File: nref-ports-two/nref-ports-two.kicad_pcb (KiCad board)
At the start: 2 copper layers, 87.5 x 40.2 mm, 111 parts, among them J1 USB_C_Receptacle, J2 USB_C_Receptacle, J3 USB3_A, J4 HD0919MSMTTR, J5 Conn_01x20, J6 Conn_01x12_Pin, U1 TUSB8041, U10 TPD4E02B04DQA, U11 TPD12S521, U12 LM2830XQMFE/NOPB, U13 LM2830XQMFE/NOPB, U2 HD3SS3220IRNHT, U3 TPD4E02B04DQA, U4 TPD4E02B04DQA, U5 TPD4E02B04DQA, U6 TPD4E02B04DQA, U7 TPD4E02B04DQA, U8 TPD4E02B04DQA, U9 TPD4E02B04DQA, Y1 24MHz

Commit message: ports-two: hdmi routing snapshot
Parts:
- removed R19, R20: 0, Resistor_SMD:R_0402_1005Metric
- added R39: 22k, Resistor_SMD:R_0402_1005Metric, F.Cu at (123.7, 60.5)
- added R40: 22k, Resistor_SMD:R_0402_1005Metric, F.Cu at (123.7, 62.5)
- added R43: 22k, Resistor_SMD:R_0402_1005Metric, F.Cu at (123.7, 64.5)
- added R44: 22k, Resistor_SMD:R_0402_1005Metric, F.Cu at (123.7, 66.5)
- added TP1: TestPoint, TestPoint:TestPoint_Pad_1.0x1.0mm, F.Cu at (126.7, 61.0)
- added TP2: TestPoint, TestPoint:TestPoint_Pad_1.0x1.0mm, F.Cu at (126.7, 64.1)
- H1, H2: value MountingHole_2.2mm_M2_Pad -> MountingHole_Pad
- moved R27 19.6 mm to (109.1, 109.2)
- moved R32 18.5 mm to (109.1, 102.6), turned to 180 degrees
- moved D1 18.4 mm to (107.1, 109.1), turned to -90 degrees
- moved R34 17.1 mm to (109.1, 101.5), turned to 180 degrees
- moved R28 16.7 mm to (109.1, 105.9)
- moved R31 16.4 mm to (109.1, 104.8), turned to 180 degrees
- moved C38 16.3 mm to (121.2, 96.5), turned to 180 degrees
- moved R29 15.4 mm to (109.1, 108.1)
- moved R33 14.7 mm to (109.1, 103.7), turned to 180 degrees
- moved R30 14.6 mm to (109.1, 107.0), turned to 180 degrees
- moved C37 13.0 mm to (121.7, 98.9)
- moved C35 9.71 mm to (122.4, 101.3), turned to -90 degrees
- moved R26 8.41 mm to (121.2, 100.4), turned to -90 degrees
- moved R1 8.33 mm to (110.2, 111.8), turned to 180 degrees
- moved U11 4.77 mm to (116.9, 105.8)
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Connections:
- H1 pad 1: (no net) -> GND
- H2 pad 1: (no net) -> GND
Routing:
- net Net-(J4-CEC): track 0.00 -> 58.8 mm, vias 0 -> 1
- net Net-(J4-SCL): track 0.00 -> 50.3 mm, vias 0 -> 1
- net Net-(J4-HPD): track 0.00 -> 46.1 mm, vias 0 -> 1
- net +5V: track 0.00 -> 39.9 mm, vias 0 -> 2
- net HDMI_TX2N: track 0.00 -> 38.1 mm, vias 0 -> 1
- net Net-(J4-SDA): track 0.00 -> 37.7 mm, vias 0 -> 1
- net HDMI_TX2P: track 0.00 -> 36.2 mm, vias 0 -> 1
- net HDMI_TX0N: track 0.00 -> 36.2 mm
- net HDMI_TX0P: track 0.00 -> 34.4 mm
- net HDMI_TX1P: track 0.00 -> 29.0 mm, vias 0 -> 1
- net HDMI_TX1N: track 0.00 -> 28.2 mm, vias 0 -> 1
- net HDMI_CLKN: track 0.00 -> 25.6 mm, vias 0 -> 1
- net +3V3: track 0.00 -> 25.1 mm, vias 0 -> 2
- net HDMI_CLKP: track 0.00 -> 24.7 mm, vias 0 -> 1
- net GND: track 0.00 -> 23.3 mm, vias 0 -> 21
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- added copper zone on B.Cu, net GND
- added copper zone on F.Cu, net GND
- added copper zone on In1.Cu, net GND
- added copper zone on In2.Cu, net GND
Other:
- copper layers 2 -> 4

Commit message: ports two: usb snapshot
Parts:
- moved R36 55.7 mm to (128.8, 115.7), turned to 180 degrees
- moved C41 55.2 mm to (130.8, 116.7), turned to -90 degrees
- moved U13 52.4 mm to (128.8, 112.7), turned to -90 degrees
- moved R42 49.6 mm to (134.3, 114.2), turned to -90 degrees
- moved D3 49.4 mm to (132.3, 112.7), turned to -90 degrees
- moved R41 46.6 mm to (134.3, 111.7), turned to -90 degrees
- moved L2 45.8 mm to (131.3, 108.7), turned to 0 degrees
- moved TP1 43.6 mm to (131.7, 104.3)
- moved C42 41.7 mm to (135.3, 108.2), turned to 90 degrees
- moved TP2 40.4 mm to (129.6, 104.3)
- moved R39 29.9 mm to (143.2, 83.2), turned to 180 degrees
- moved FB1 29.7 mm to (183.3, 109.8), turned to 0 degrees
- moved C24 29.5 mm to (147.7, 104.6), turned to -90 degrees
- moved C22 28.5 mm to (146.7, 104.6), turned to -90 degrees
- moved R3 27.7 mm to (164.1, 117.2)
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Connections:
- J6 pad 1: USB2A_DN -> USB2_DN
- J6 pad 2: USB2A_DP -> USB2_DP
- U1 pad 19: USBH_1B_TXN -> USBH_2B_TXP
- U1 pad 20: USBH_1B_TXP -> USBH_2B_TXN
- U1 pad 22: USBH_1B_RXN -> USBH_2B_RXN
- U1 pad 23: USBH_1B_RXP -> USBH_2B_RXP
- U1 pad 26: USBH_2B_TXN -> USBH_1B_TXP
- U1 pad 27: USBH_2B_TXP -> USBH_1B_TXN
- U1 pad 29: USBH_2B_RXN -> USBH_1B_RXN
- U1 pad 30: USBH_2B_RXP -> USBH_1B_RXP
- U5 pad 4: /USBH_2B_AC_TXN -> /USBH_2B_AC_TXP
- U5 pad 5: /USBH_2B_AC_TXP -> /USBH_2B_AC_TXN
- U5 pad 6: /USBH_2B_AC_TXP -> /USBH_2B_AC_TXN
- U5 pad 7: /USBH_2B_AC_TXN -> /USBH_2B_AC_TXP
- U9 pad 4: USBH_1A_RXN -> USBH_1A_RXP
- U9 pad 5: USBH_1A_RXP -> USBH_1A_RXN
- U9 pad 6: USBH_1A_RXP -> USBH_1A_RXN
- U9 pad 7: USBH_1A_RXN -> USBH_1A_RXP
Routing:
- net USBH_1_DP: track 0.00 -> 63.6 mm, vias 0 -> 3
- net USBH_1_DN: track 0.00 -> 62.7 mm, vias 0 -> 1
- net USBH_2B_RXP: track 0.00 -> 53.6 mm, vias 0 -> 2
- net USBH_2B_RXN: track 0.00 -> 52.7 mm, vias 0 -> 2
- net USBH_2A_RXN: track 0.00 -> 51.7 mm, vias 0 -> 4
- net USBH_2A_RXP: track 0.00 -> 50.4 mm, vias 0 -> 4
- net /USBH_2B_AC_TXN: track 0.00 -> 47.1 mm, vias 0 -> 2
- net /USBH_2B_AC_TXP: track 0.00 -> 45.6 mm, vias 0 -> 2
- net USBH_2_DN: track 0.00 -> 45.2 mm, vias 0 -> 4
- net USBH_2_DP: track 0.00 -> 42.0 mm, vias 0 -> 2
- net /USBH_2A_AC_TXN: track 0.00 -> 41.8 mm, vias 0 -> 2
- net /USBH_2A_AC_TXP: track 0.00 -> 40.5 mm, vias 0 -> 2
- net USBH_3_DN: track 0.00 -> 32.0 mm, vias 0 -> 2
- net USBH_3_DP: track 0.00 -> 30.3 mm, vias 0 -> 2
- net USBH_1B_RXP: track 0.00 -> 27.1 mm
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
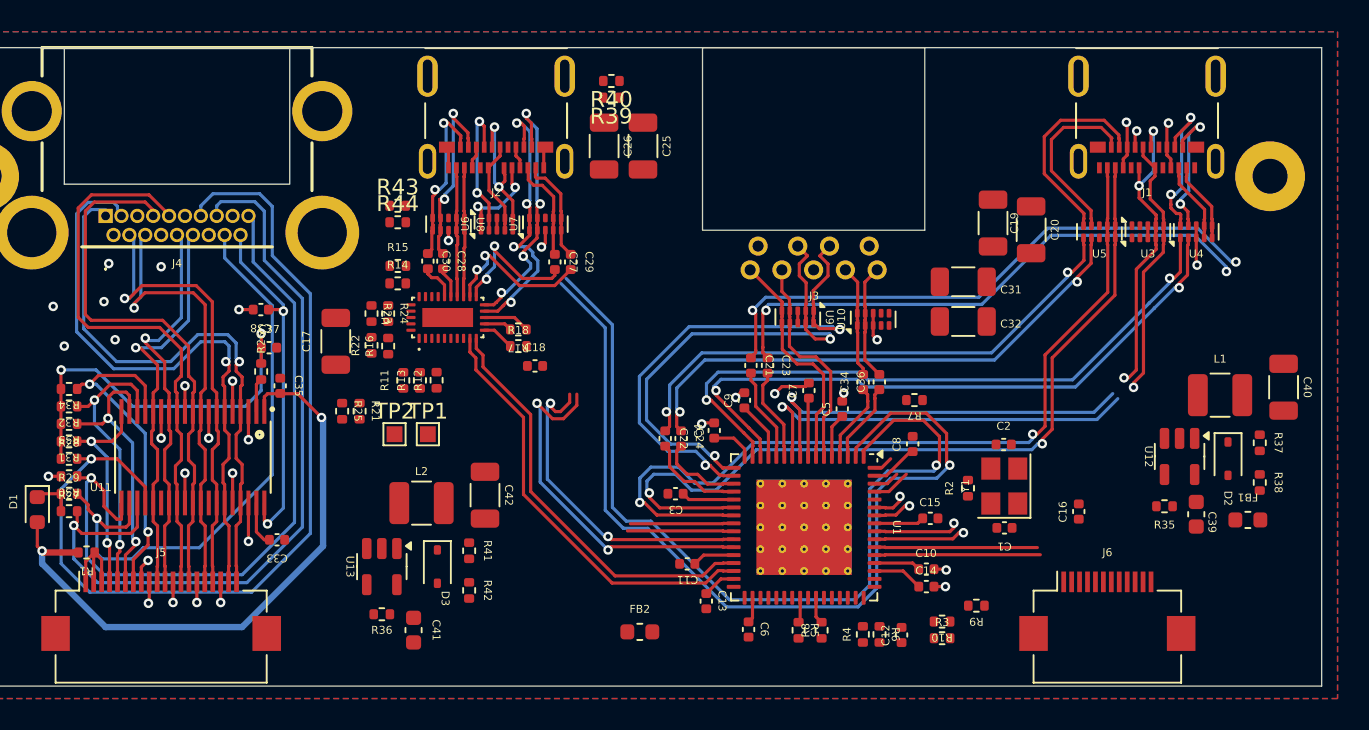
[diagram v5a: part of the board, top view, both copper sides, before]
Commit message: port board two fully routed
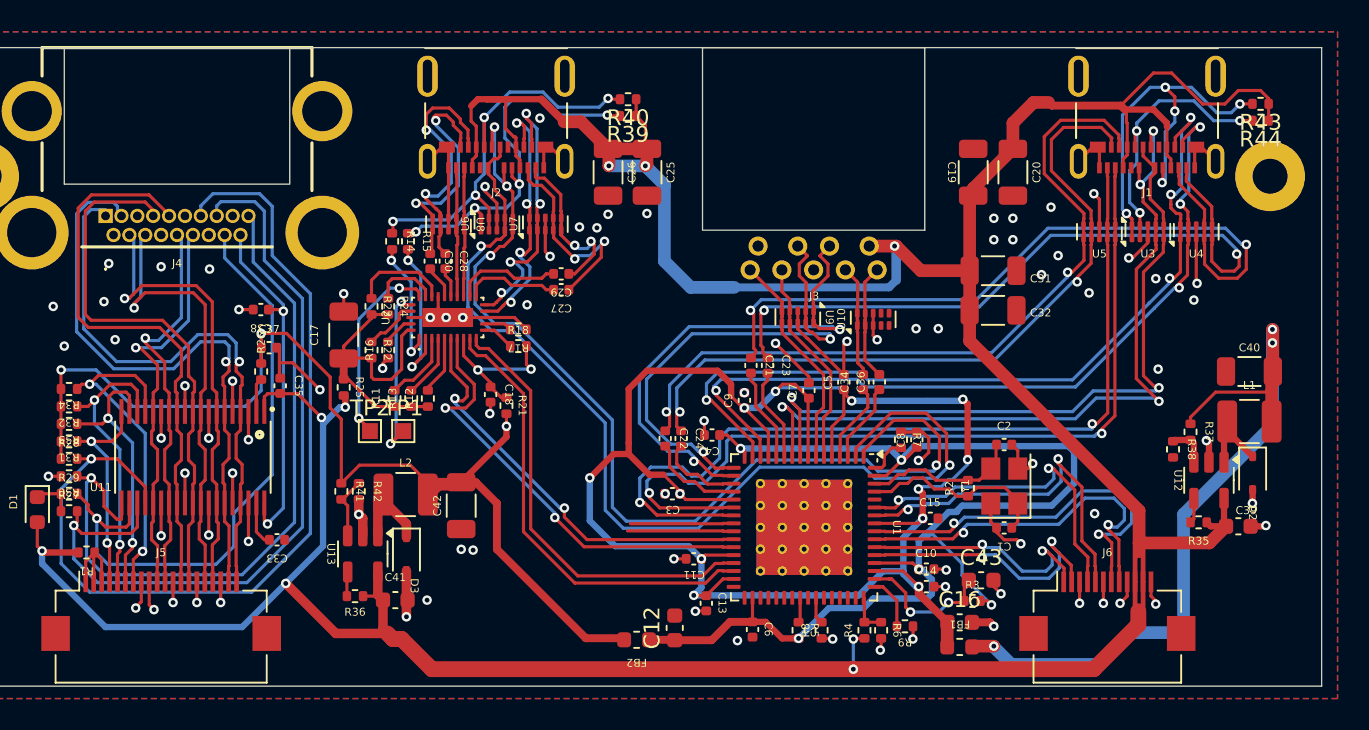
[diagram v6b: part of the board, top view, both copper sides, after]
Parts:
- removed R10: 0, Resistor_SMD:R_0402_1005Metric
- added C43: 10uF, Capacitor_SMD:C_0603_1608Metric, F.Cu at (166.6, 113.5)
- C12, C16: footprint Capacitor_SMD:C_0402_1005Metric -> Capacitor_SMD:C_0603_1608Metric
- R3: value 100k -> 1M
- moved R43 54.7 mm to (184.2, 83.5), turned to 180 degrees
- moved R44 54.7 mm to (184.2, 84.6), turned to 180 degrees
- moved FB1 19.8 mm to (165.2, 117.8)
- moved C12 14.3 mm to (147.2, 116.5)
- moved C16 10.2 mm to (165.2, 116.2), turned to 0 degrees
- moved R42 9.34 mm to (127.3, 108.0)
- moved R21 9.26 mm to (136.7, 102.5)
- moved R41 8.88 mm to (126.2, 108.0)
- moved R38 5.85 mm to (178.6, 105.3)
- moved R9 4.68 mm to (161.8, 116.5)
- moved R37 4.42 mm to (179.7, 104.2)
- moved C20 3.80 mm to (168.6, 87.8)
- moved C19 3.44 mm to (166.1, 87.8), turned to 90 degrees
- moved C18 3.33 mm to (135.7, 101.8), turned to -90 degrees
- moved R3 3.03 mm to (166.0, 114.8)
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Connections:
- J2 pad A5: Net-(J2-CC1) -> MUXCC1
- J2 pad B5: Net-(J2-CC2) -> MUXCC2
- R14 pad 1: CC2 -> MUXCC2
- R15 pad 1: CC1 -> MUXCC1
- R3 pad 2: GND -> USBH_3V3
- R39 pad 2: Net-(J2-CC1) -> MUXCC1
- R40 pad 2: Net-(J2-CC2) -> MUXCC2
- U1 pad 50: Net-(U1-GRSTz) -> ~{USBH_RESET}
- U6 pad 1: Net-(J2-CC1) -> MUXCC1
- U6 pad 10: Net-(J2-CC1) -> MUXCC1
- U6 pad 2: Net-(J2-CC2) -> MUXCC2
- U6 pad 9: Net-(J2-CC2) -> MUXCC2
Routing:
- net +5V: track 48.7 -> 250.8 mm, vias 4 -> 9
- net USBH_1V1: track 24.7 -> 112.7 mm, vias 0 -> 12
- net GND: track 43.4 -> 121.6 mm, vias 31 -> 87
- net USBH_3V3: track 10.3 -> 77.4 mm, vias 0 -> 5
- net +1V1: track 0.00 -> 47.9 mm, vias 0 -> 3
- net +3V3: track 25.1 -> 68.7 mm, vias 2 -> 3
- net MUXCC2: track 0.00 -> 26.1 mm, vias 0 -> 4
- net CC1: track 0.00 -> 25.3 mm, vias 0 -> 5
- net MUXCC1: track 0.00 -> 24.6 mm, vias 0 -> 4
- net USB2_TXP: track 2.45 -> 23.0 mm, vias 1 -> 2
- net MUX_5V: track 0.00 -> 19.9 mm
- net USB2_TXN: track 2.08 -> 21.5 mm, vias 1 -> 2
- net USB2_RXN: track 5.40 -> 24.8 mm, vias 1 -> 2
- net USB2_RXP: track 5.77 -> 23.1 mm, vias 1 -> 2
- net CC2: track 1.06 -> 17.1 mm, vias 1 -> 3
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
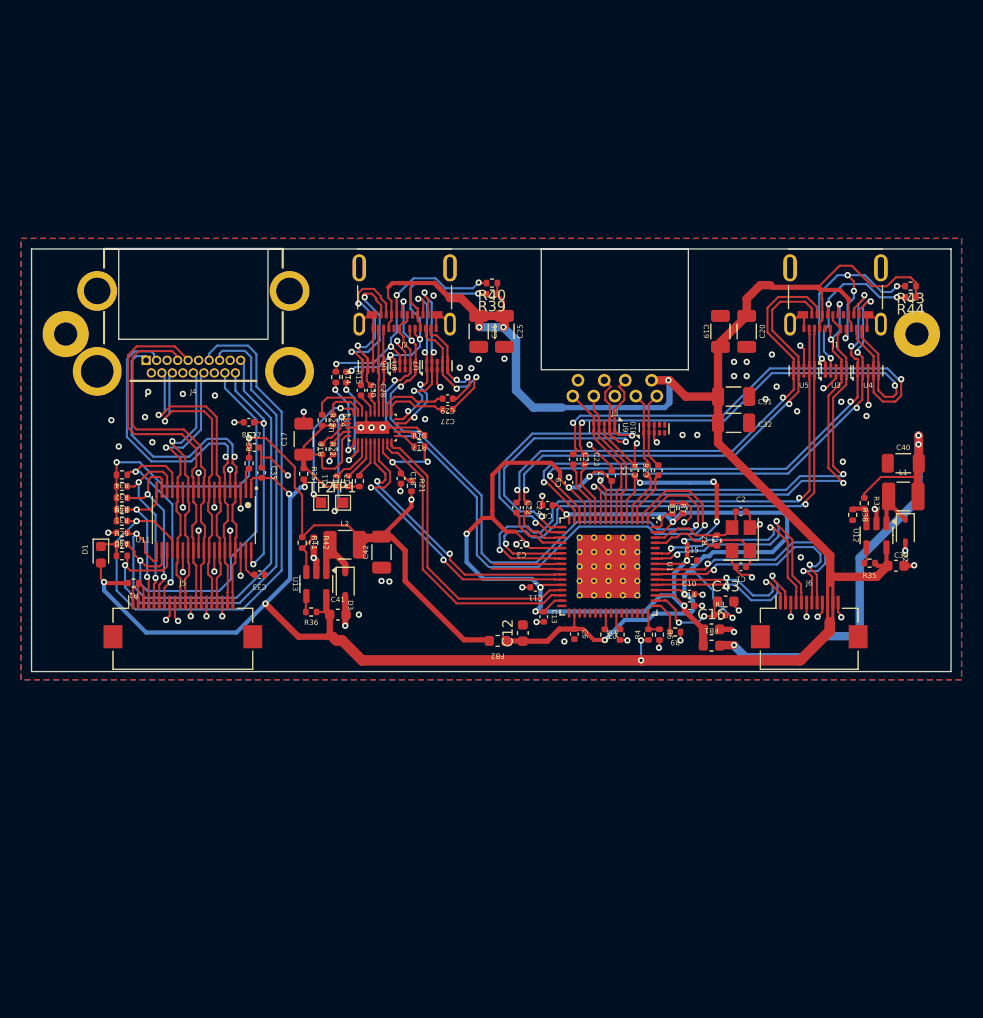
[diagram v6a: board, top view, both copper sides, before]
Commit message: ports two bom adjustments
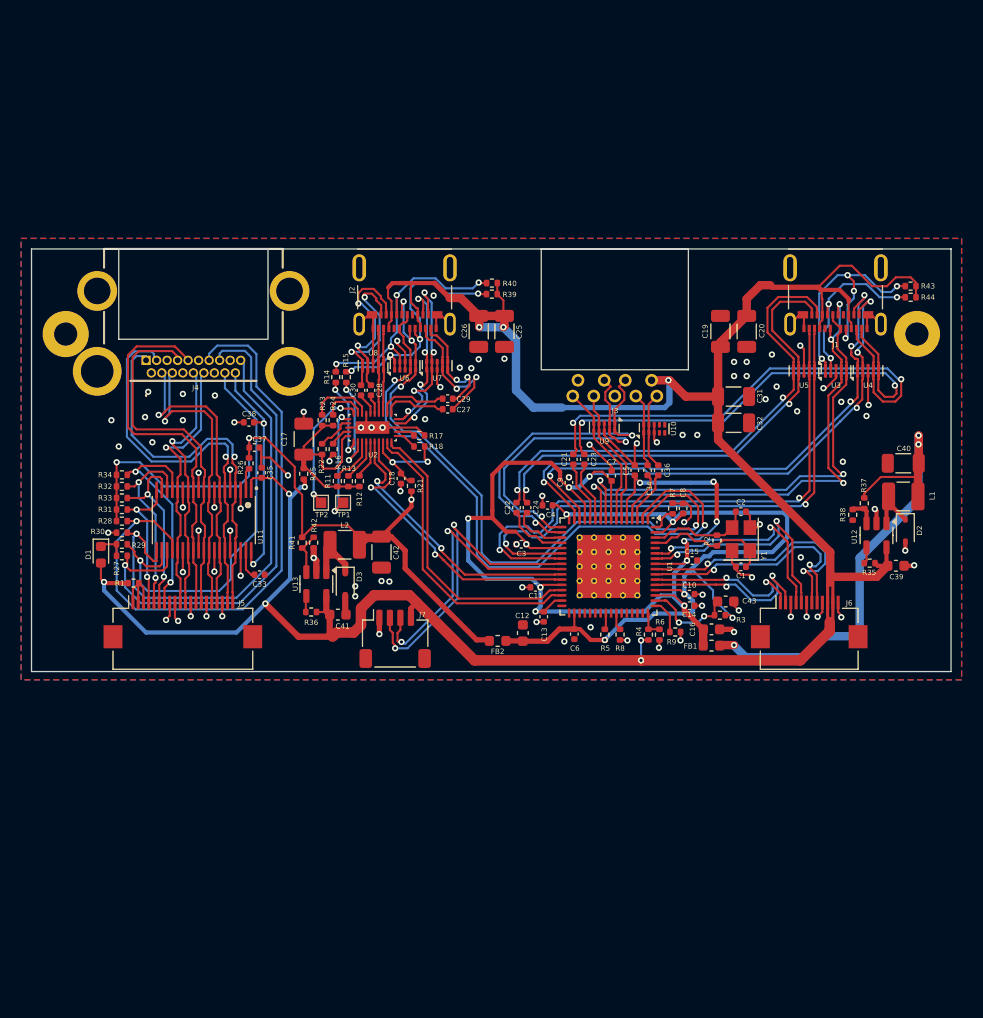
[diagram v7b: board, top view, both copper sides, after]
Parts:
- added H3: BADGE, footprints:nref-ports-two-badge, B.Cu at (183.0, 105.2)
- added J7: Conn_01x04, Connector_JST:JST_SH_SM04B-SRSS-TB_1x04-1MP_P1.00mm_Horizontal, F.Cu at (135.1, 117.1)
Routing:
- net USBH_4_DP: track 6.51 -> 30.1 mm, vias 0 -> 2
- net USBH_4_DN: track 6.70 -> 28.5 mm, vias 0 -> 2
- net +5V: track 250.8 -> 256.6 mm
- net +3V3: track 68.7 -> 68.0 mm
- net GND: track 121.6 -> 122.1 mm, vias 87 -> 90
